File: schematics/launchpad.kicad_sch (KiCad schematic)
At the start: 19 parts

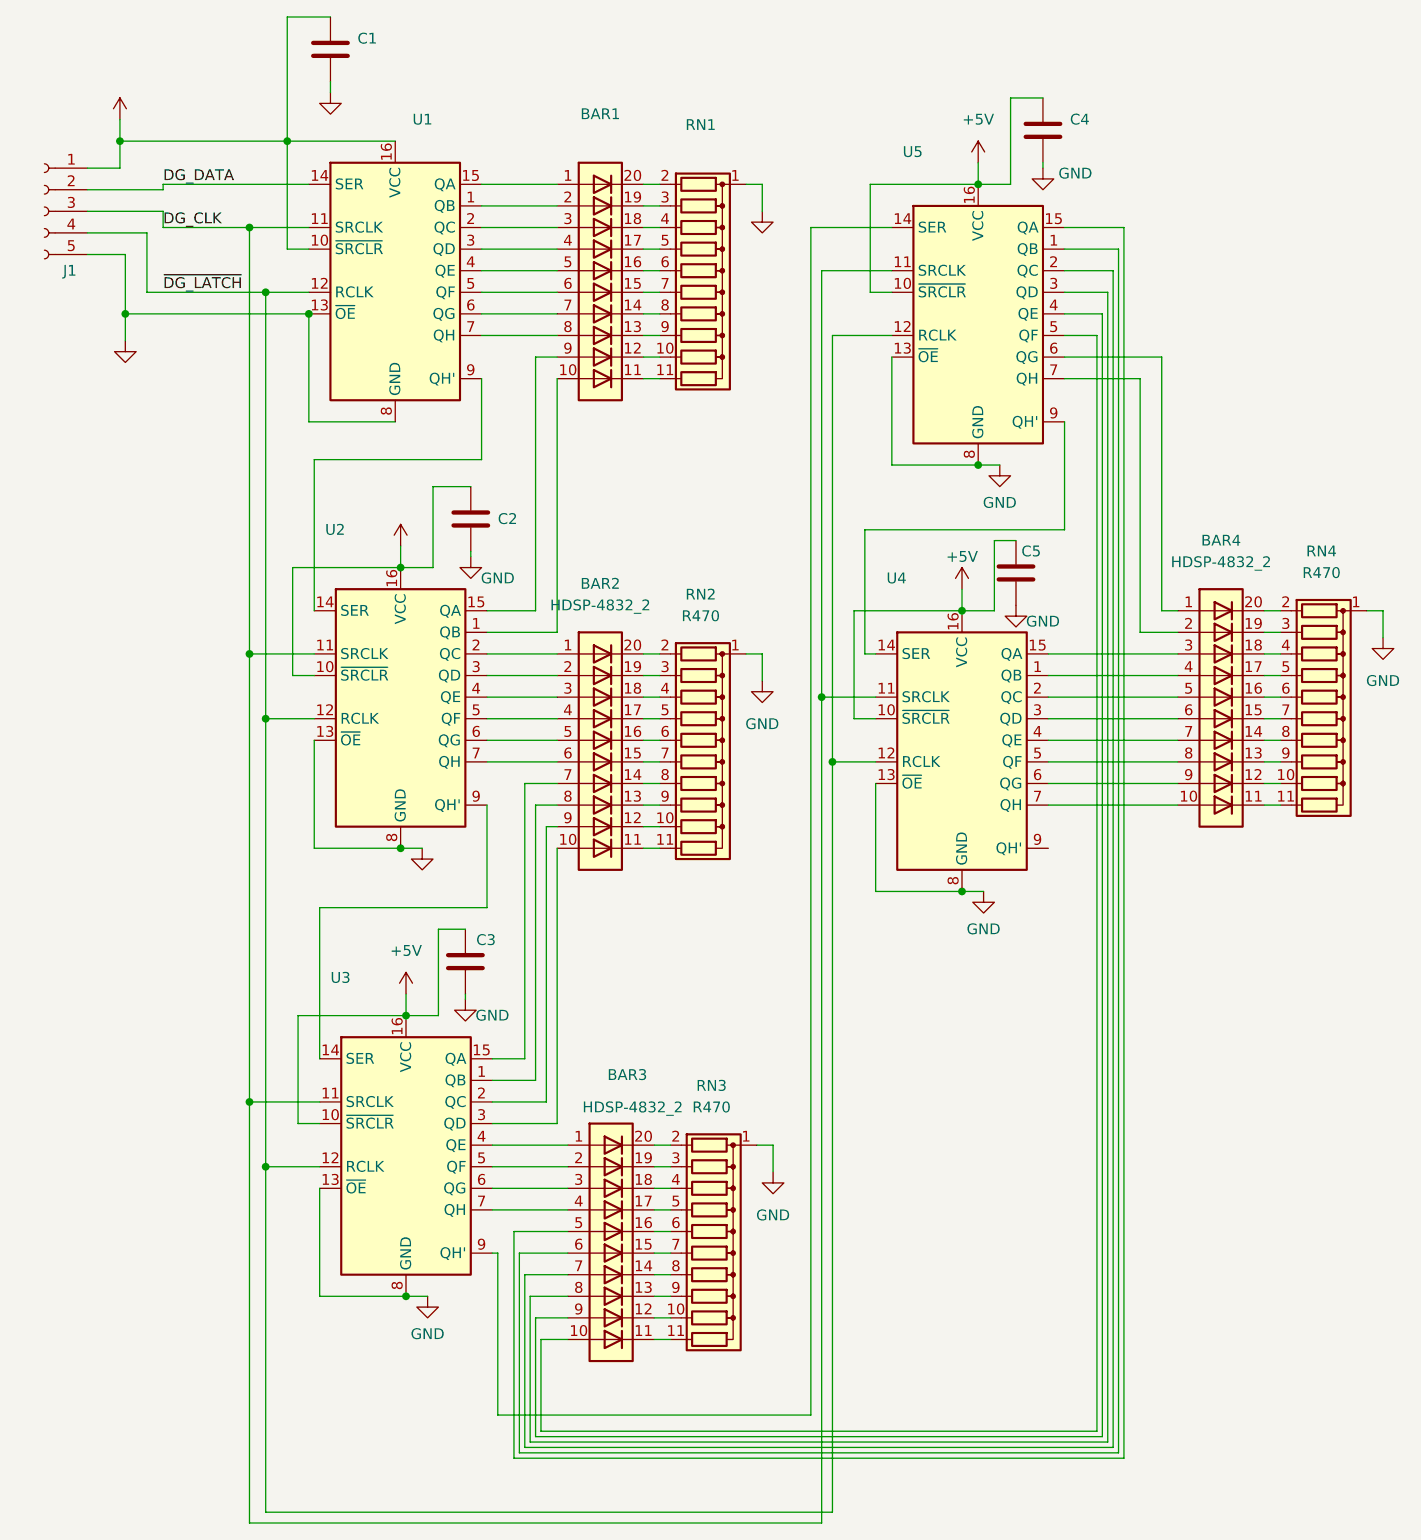
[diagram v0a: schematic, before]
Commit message: SCH: Gauges routing complete
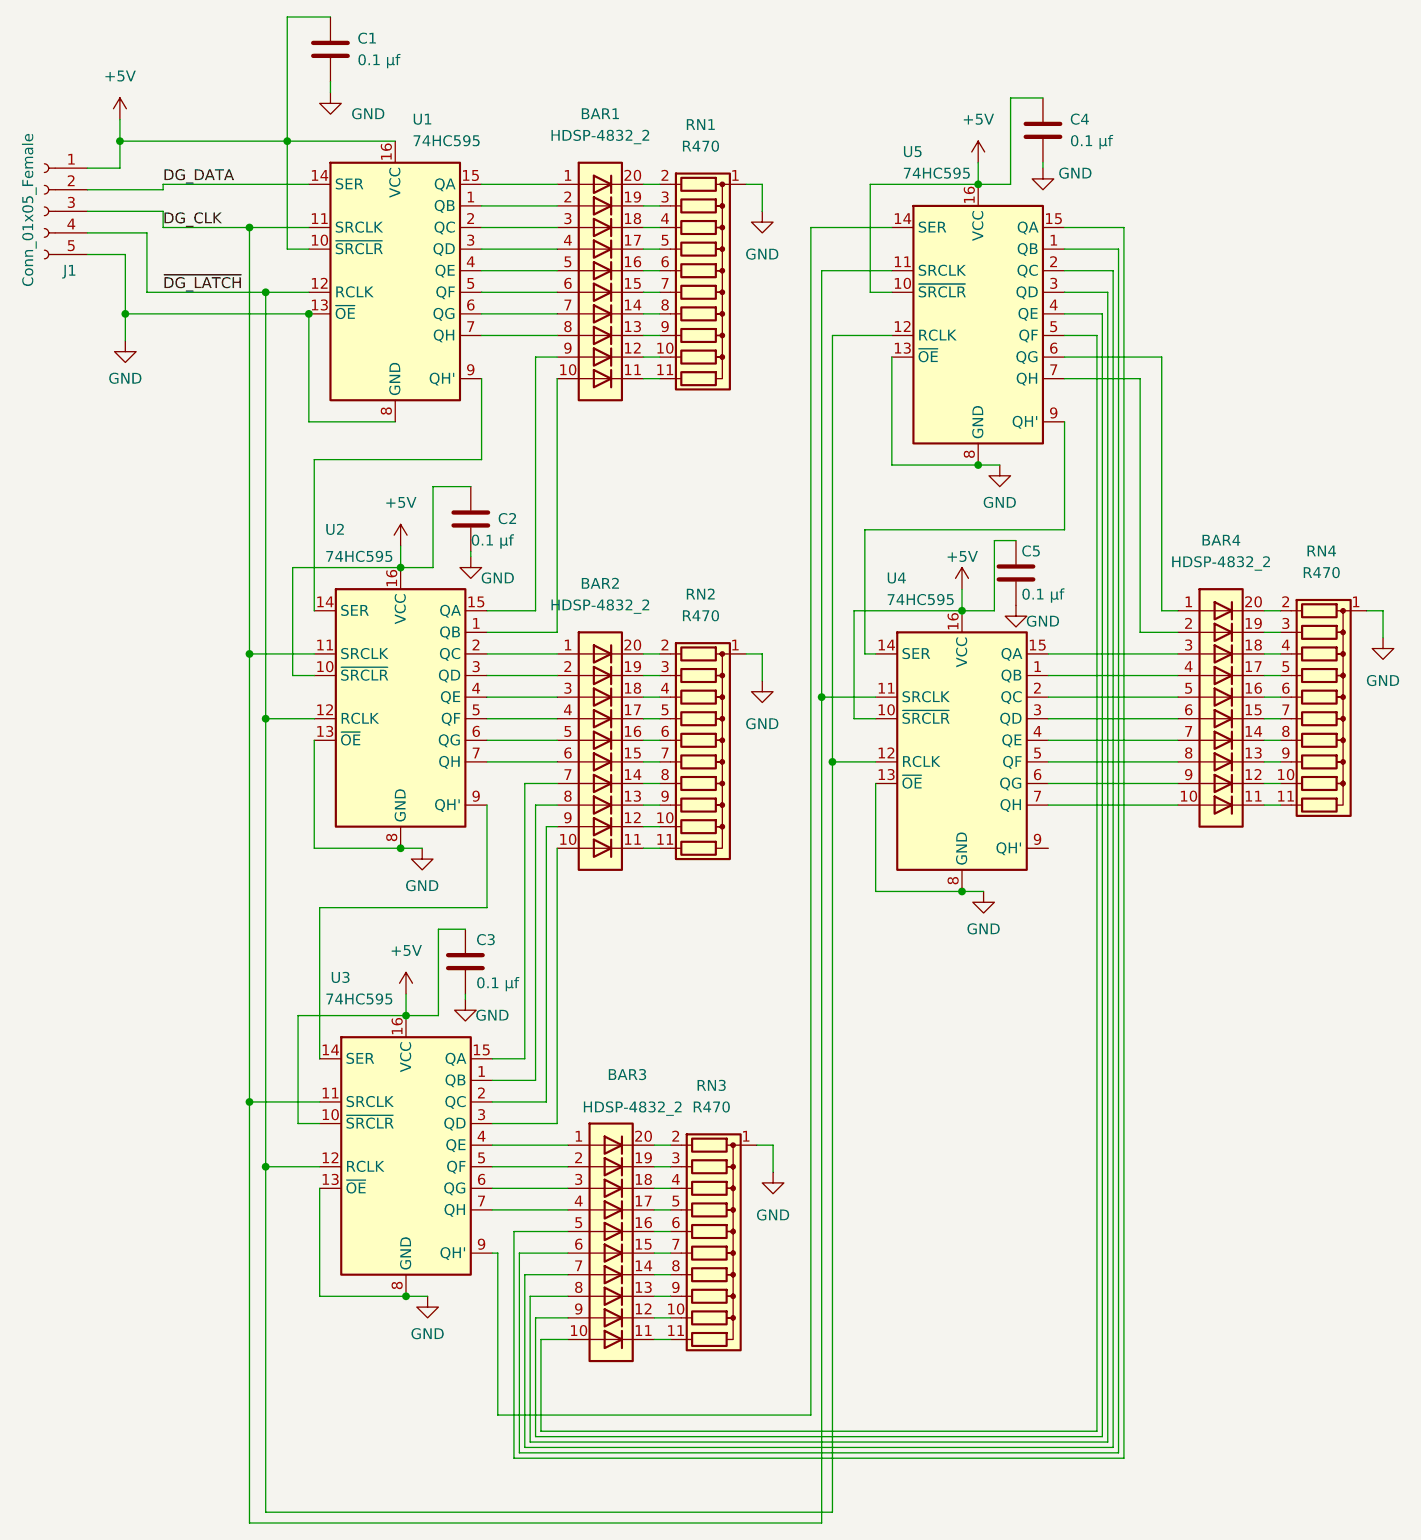
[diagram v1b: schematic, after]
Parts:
- BAR1: value (none) -> HDSP-4832_2; footprint (none) -> Display:HDSP-4832
- C1, C2, C3, C4, C5: value (none) -> 0.1 µf; footprint (none) -> Capacitor_THT:C_Disc_D4.3mm_W1.9mm_P5.00mm; LCSC (none) -> C254085
- J1: value (none) -> Conn_01x05_Female; footprint (none) -> Connectors_JST:JST_EH_B05B-EH-A_05x2.50mm_Straight
- RN1: value (none) -> R470; footprint (none) -> Resistor_THT:R_Array_SIP11
- U1, U2, U3, U4, U5: value (none) -> 74HC595; footprint (none) -> Package_DIP:DIP-16_W7.62mm

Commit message: SCH: routing improvement
+ground plane
+via stiching
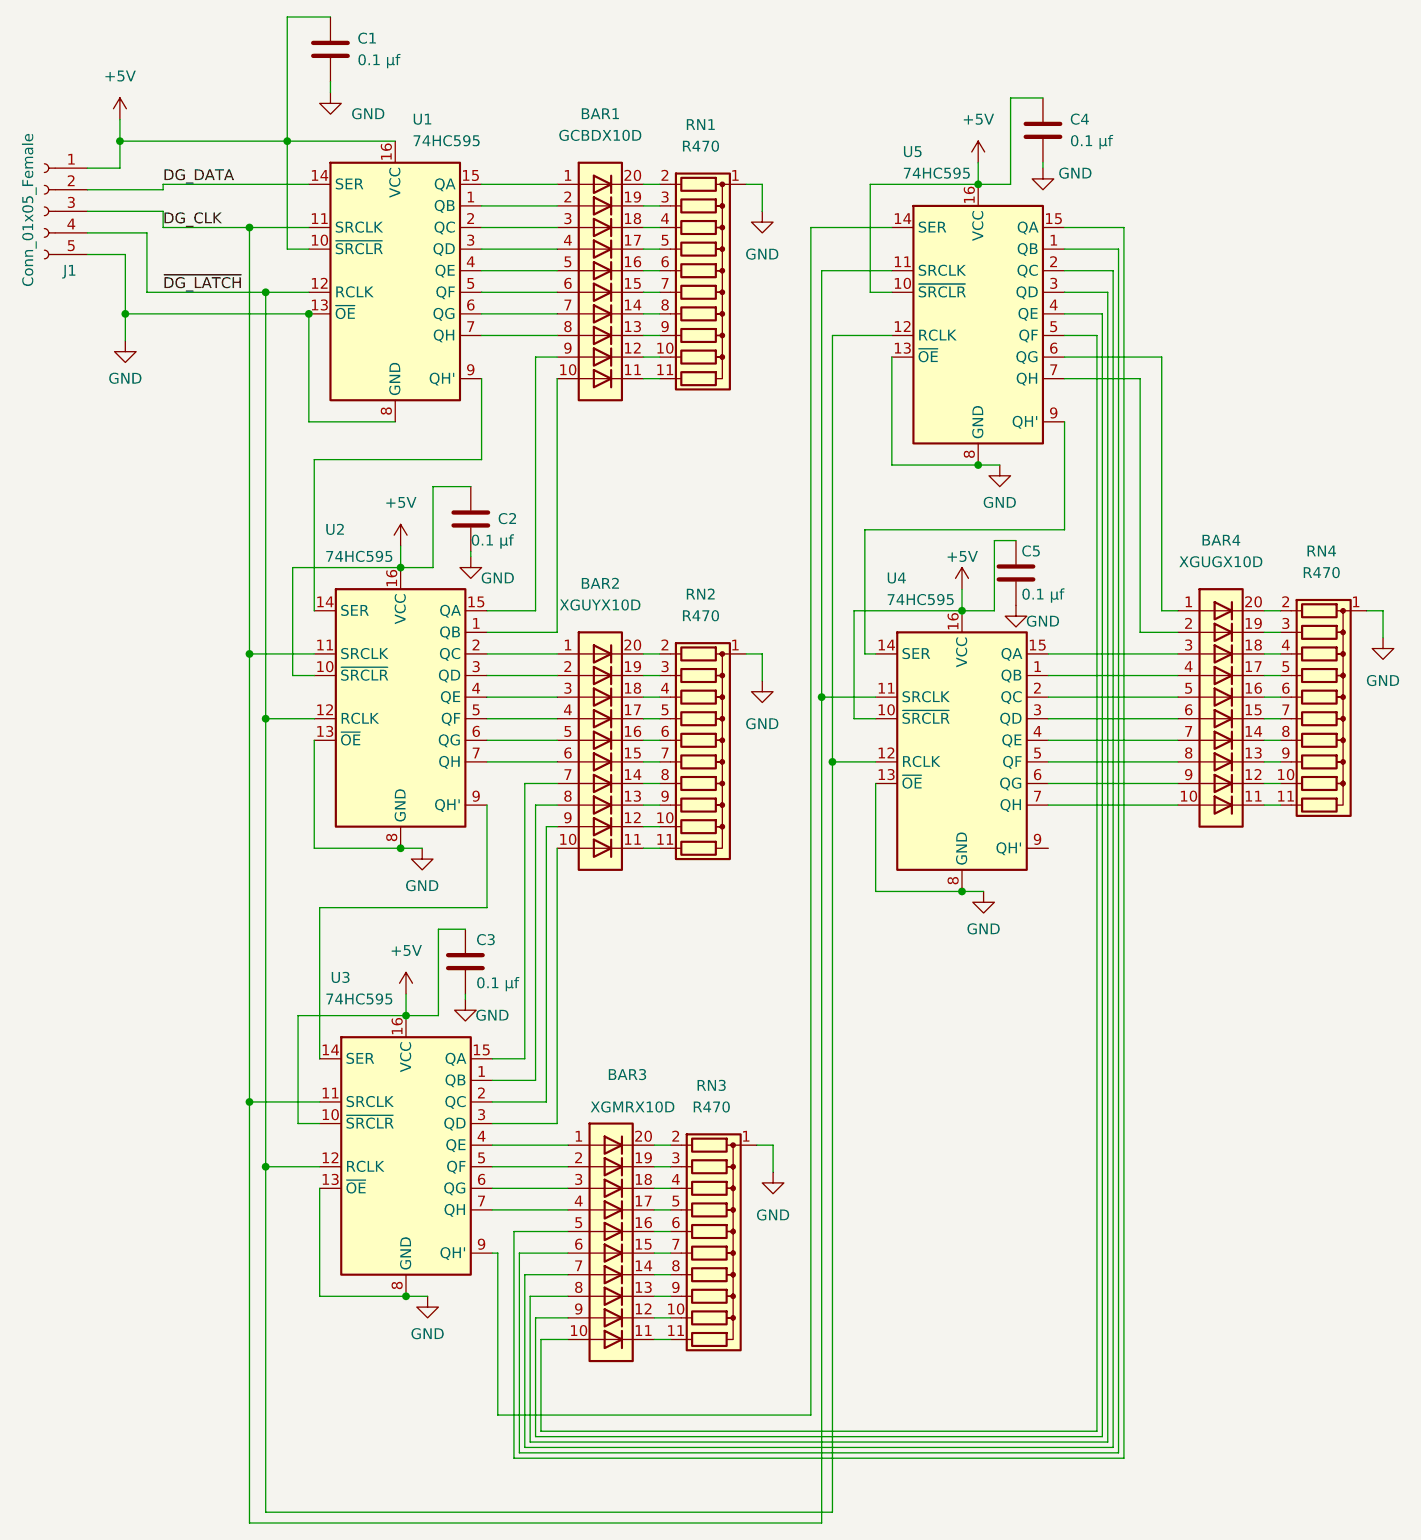
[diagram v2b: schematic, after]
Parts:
- BAR1: value HDSP-4832_2 -> GCBDX10D
- BAR2: value HDSP-4832_2 -> XGUYX10D
- BAR3: value HDSP-4832_2 -> XGMRX10D
- BAR4: value HDSP-4832_2 -> XGUGX10D
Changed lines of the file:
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@@
       (effects (font (size 1.27 1.27)))
     )
-    (property "Value" "HDSP-4832_2" (at 81.28 86.995 0)
+    (property "Value" "XGUYX10D" (at 81.28 86.995 0)
       (effects (font (size 1.27 1.27)))
     )
@@
       (effects (font (size 1.27 1.27)))
     )
-    (property "Value" "HDSP-4832_2" (at 81.28 31.75 0)
+    (property "Value" "GCBDX10D" (at 81.28 31.75 0)
       (effects (font (size 1.27 1.27)))
     )
@@
       (effects (font (size 1.27 1.27)))
     )
-    (property "Value" "HDSP-4832_2" (at 154.305 81.915 0)
+    (property "Value" "XGUGX10D" (at 154.305 81.915 0)
       (effects (font (size 1.27 1.27)))
     )
@@
       (effects (font (size 1.27 1.27)))
     )
-    (property "Value" "HDSP-4832_2" (at 85.09 146.05 0)
-      (effects (font (size 1.27 1.27)))
-    )
+    (property "Value" "XGMRX10D" (at 85.09 146.05 0)
+      (effects (font (size 1.27 1.27)))
+    )
